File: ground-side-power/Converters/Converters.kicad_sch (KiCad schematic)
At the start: 29 parts, among them J10 Conn_01x03_Female, J11 Ground Connections, J12 Conn_01x04_Female, J13 DAQ Voltage Sensing, J14 DAQ Current Sensing, J27 Conn_01x02_Female, U1 TPS55340, U4 INA180, U5 INA180

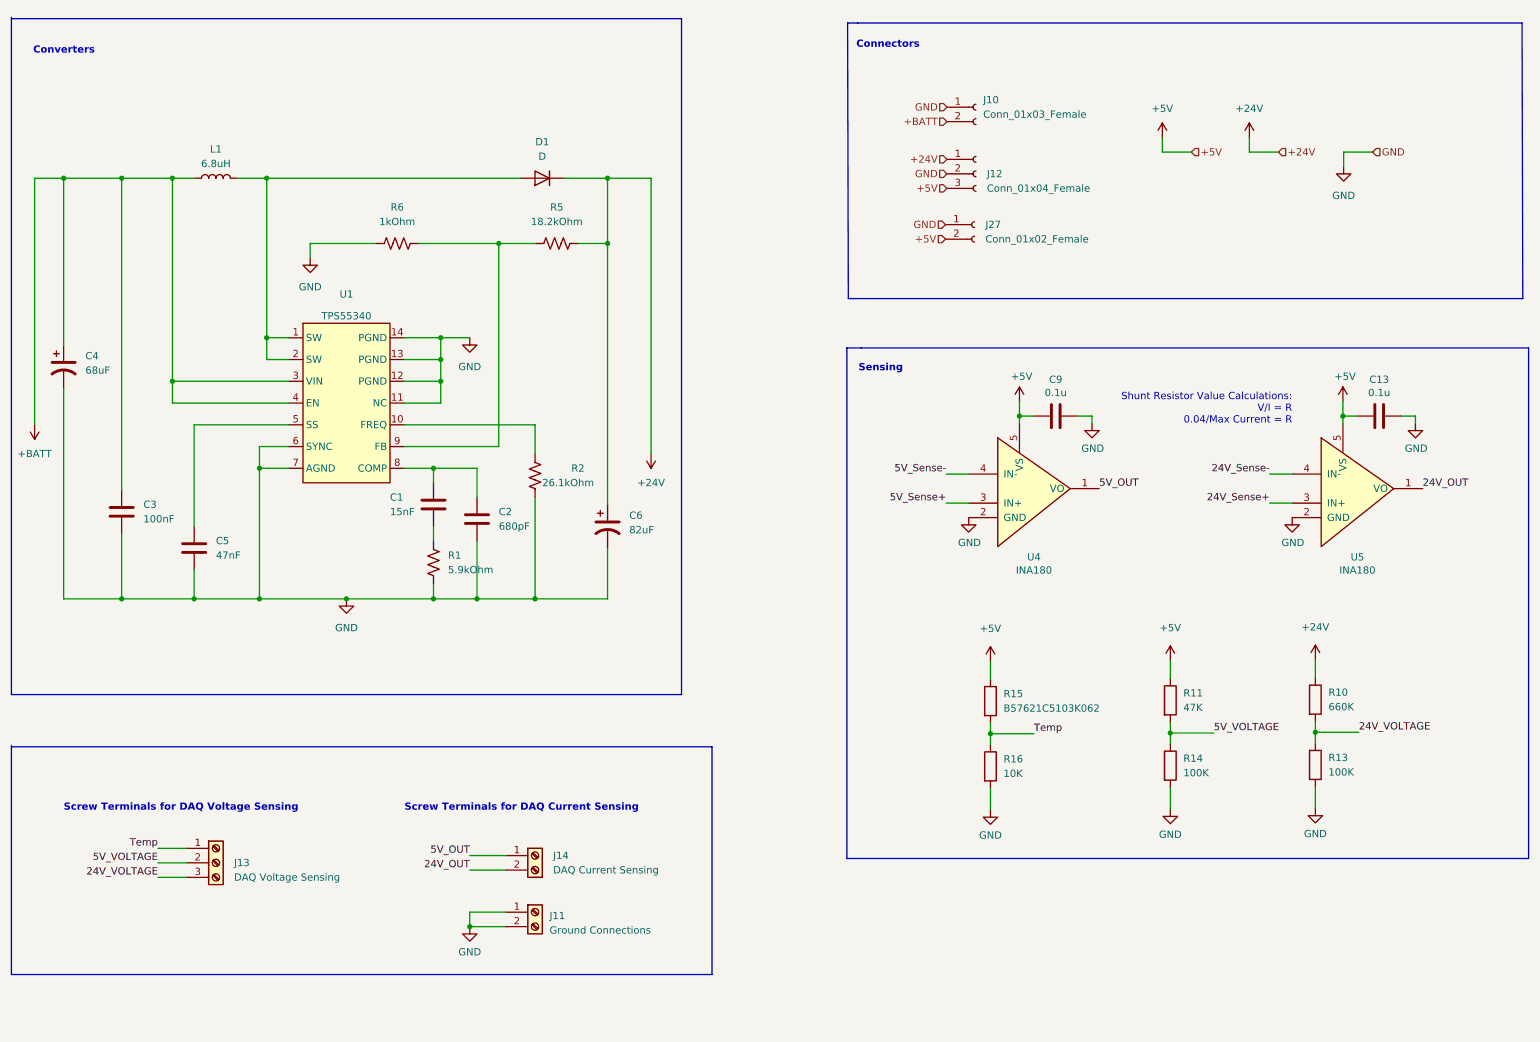
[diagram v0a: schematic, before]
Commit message: undeleted 5v regulator
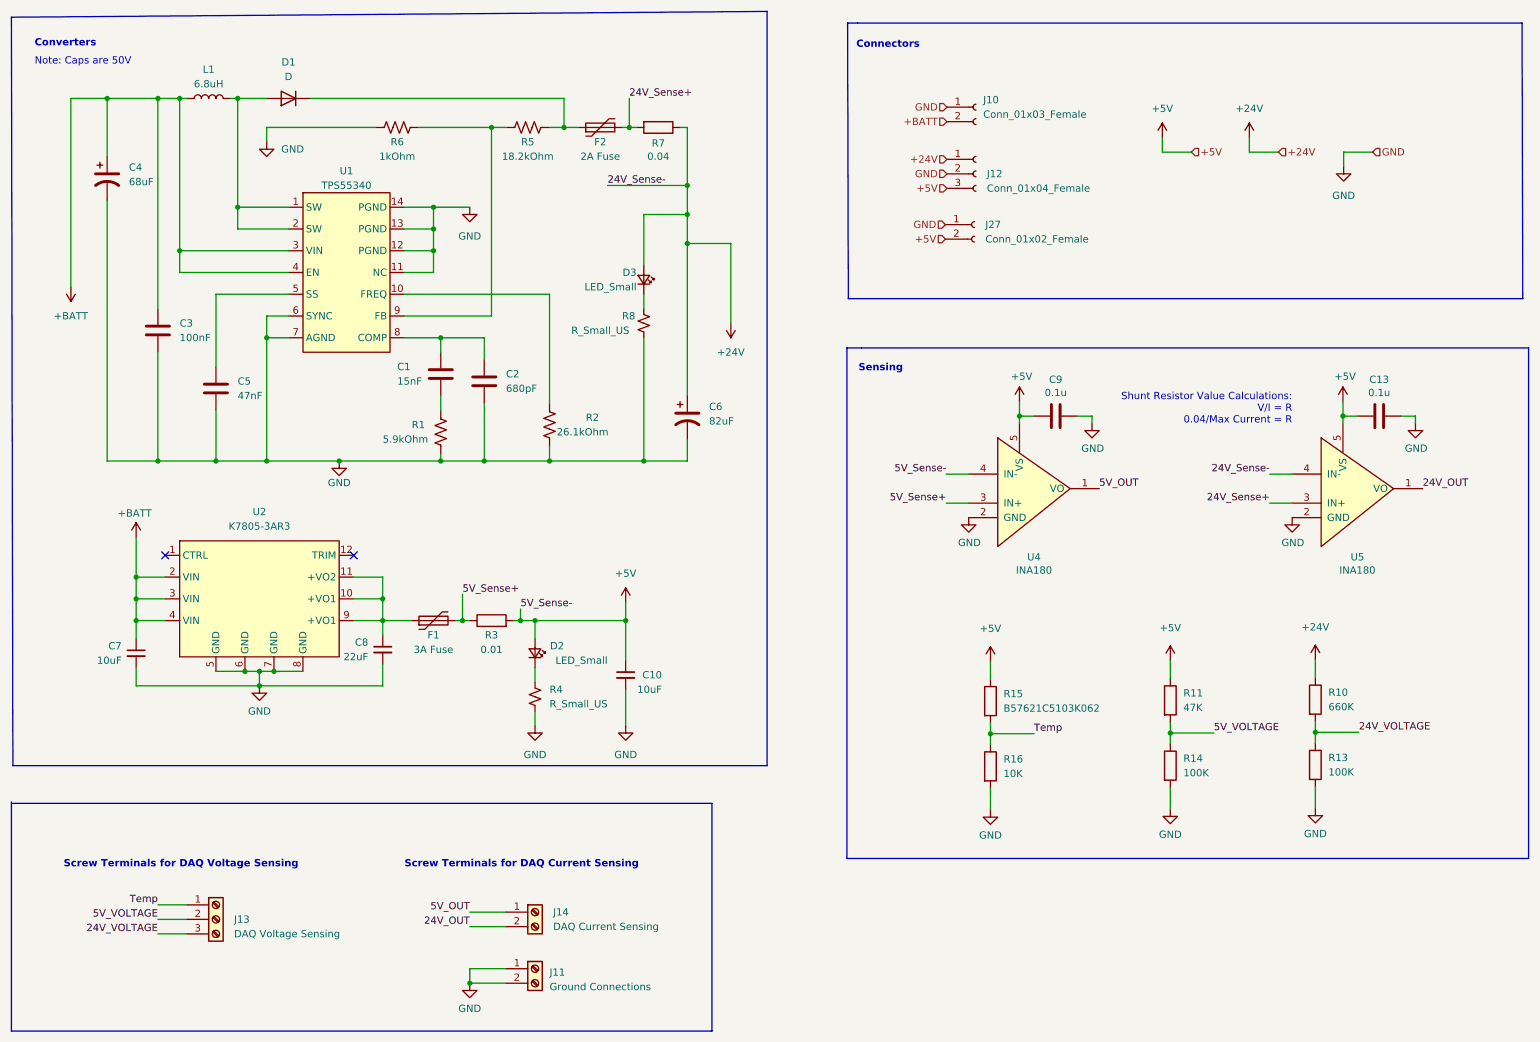
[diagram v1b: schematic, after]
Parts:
- added C10, C7: 10uF, Capacitor_SMD:C_0805_2012Metric_Pad1.18x1.45mm_HandSolder, symbol Device:C_Small
- added C8: 22uF, Capacitor_SMD:C_0805_2012Metric_Pad1.18x1.45mm_HandSolder, symbol Device:C_Small
- added D2, D3: LED_Small, Diode_SMD:D_1206_3216Metric_Pad1.42x1.75mm_HandSolder, symbol Device:LED_Small
- added F1: 3A Fuse, Fuse:Fuseholder_Clip-6.3x32mm_Littelfuse_102_122_Inline_P34.21x7.62mm_D1.98mm_Horizontal, symbol Device:Polyfuse
- added F2: 2A Fuse, Fuse:Fuseholder_Clip-6.3x32mm_Littelfuse_102_122_Inline_P34.21x7.62mm_D1.98mm_Horizontal, symbol Device:Polyfuse
- added R3: 0.01, Resistor_SMD:R_2512_6332Metric_Pad1.40x3.35mm_HandSolder, symbol Device:R
- added R4, R8: R_Small_US, Resistor_SMD:R_0805_2012Metric_Pad1.20x1.40mm_HandSolder, symbol Device:R_Small_US
- added R7: 0.04, Resistor_SMD:R_2512_6332Metric_Pad1.40x3.35mm_HandSolder, symbol Device:R
- added U2: K7805-3AR3, GSP:K7805-3AR3, symbol Regulator_Switching:AP63203WU
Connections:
- net 24V_Sense- is gone; now on net +24V: U5.4 (IN-)
- net 5V_Sense- is gone; now on net +5V: U4.4 (IN-)
- net +24V: now also D3.2 (A), R7.1; no longer D1.1 (K), R5.2
- net +5V: now also C10.1, D2.2 (A), R3.2
- net +BATT: now also C7.1, U2.2 (VIN), U2.3 (VIN), U2.4 (VIN)
- net 24V_Sense+: now also F2.2, R7.2
- net 5V_Sense+: now also F1.2, R3.1
- net GND: now also C10.2, C7.2, C8.2, R4.1, R8.1, U2.5 (GND), U2.6 (GND), U2.7 (GND), U2.8 (GND)
- new net: D2.1 (K), R4.2
- new net: C8.1, F1.1, U2.10 (+VO1), U2.11 (+VO2), U2.9 (+VO1)
- new net: D1.1 (K), F2.1, R5.2
- new net: D3.1 (K), R8.2
- no-connect marks 0 -> 2
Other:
- note added: "Note: Caps are 50V"
- moved on the sheet: C1, C2, C3, C4, C5, C6, D1, J11, J13, J14, L1, R1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

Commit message: implemented comments
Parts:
- removed C4: 68uF, Capacitor_SMD:C_Elec_6.3x7.7, symbol Device:C_Polarized_US
- removed C6: 82uF, Capacitor_SMD:CP_Elec_8x11.9, symbol Device:C_Polarized_US
- removed D1: D, Diode_SMD:D_SMB-SMC_Universal_Handsoldering, symbol Device:D
- removed D2, D3: LED_Small, Diode_SMD:D_1206_3216Metric_Pad1.42x1.75mm_HandSolder, symbol Device:LED_Small
- removed F1: 3A Fuse, Fuse:Fuseholder_Clip-6.3x32mm_Littelfuse_102_122_Inline_P34.21x7.62mm_D1.98mm_Horizontal, symbol Device:Polyfuse
- removed F2: 2A Fuse, Fuse:Fuseholder_Clip-6.3x32mm_Littelfuse_102_122_Inline_P34.21x7.62mm_D1.98mm_Horizontal, symbol Device:Polyfuse
- removed R10: 660K, Resistor_SMD:R_0805_2012Metric_Pad1.20x1.40mm_HandSolder, symbol Device:R
- removed R11: 47K, Resistor_SMD:R_0805_2012Metric_Pad1.20x1.40mm_HandSolder, symbol Device:R
- removed R13, R14: 100K, Resistor_SMD:R_0805_2012Metric_Pad1.20x1.40mm_HandSolder, symbol Device:R
- removed R15: B57621C5103K062, Resistor_SMD:R_1206_3216Metric_Pad1.30x1.75mm_HandSolder, symbol Device:R
- removed R16: 10K, Resistor_SMD:R_0805_2012Metric_Pad1.20x1.40mm_HandSolder, symbol Device:R
- removed R3: 0.01, Resistor_SMD:R_2512_6332Metric_Pad1.40x3.35mm_HandSolder, symbol Device:R
- removed R4, R8: R_Small_US, Resistor_SMD:R_0805_2012Metric_Pad1.20x1.40mm_HandSolder, symbol Device:R_Small_US
- removed R7: 0.04, Resistor_SMD:R_2512_6332Metric_Pad1.40x3.35mm_HandSolder, symbol Device:R
- added C11, C4, C6: 4.7uF, Capacitor_SMD:C_0805_2012Metric_Pad1.18x1.45mm_HandSolder, symbol Device:C
- added D2: SK54A-LTP, symbol Device:D_Schottky
- added D4, D5: LED, symbol Device:LED
- added F3: 0685T4000-01, symbol Device:Fuse
- added F4: 3A Fuse, symbol Device:Fuse
- added R10: 0.01R, symbol Device:R_US
- added R12: 78.7k, symbol Device:R_US
- added R17: 10k, symbol Device:R_US
- added R18: 187k, symbol Device:R_US
- added R19: 660k, symbol Device:R_US
- added R20: 100k, symbol Device:R_US
- added R3: 16mR, symbol Device:R_US
- added R4: 2k, symbol Device:R_US
- added R8, R9: R_US, symbol Device:R_US
- C1: value 15nF -> 0.1uF
- C2: value 680pF -> 100pF
- C3: value 100nF -> 10uF
- L1: value 6.8uH -> 74437368100
- R1: value 5.9kOhm -> B57621C5103K062; footprint Resistor_SMD:R_0402_1005Metric_Pad0.72x0.64mm_HandSolder -> (none)
- R2: value 26.1kOhm -> 10k; footprint Resistor_SMD:R_0402_1005Metric_Pad0.72x0.64mm_HandSolder -> (none)
- R5: value 18.2kOhm -> 47k; footprint Resistor_SMD:R_0402_1005Metric_Pad0.72x0.64mm_HandSolder -> (none)
- R6: value 1kOhm -> 100k; footprint Resistor_SMD:R_0402_1005Metric_Pad0.72x0.64mm_HandSolder -> (none)
- U1: footprint Package_SO:TSSOP-14_4.4x3.6mm_P0.4mm -> (none)
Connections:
- net +24V: now also D4.2 (A), R19.1, R3.2
- net +5V: now also R1.1, R5.1, D5.2 (A), R10.2
- net 24V_Sense+: now also F3.2, R3.1
- net 24V_VOLTAGE: now also R19.2, R20.1
- net 5V_Sense+: now also F4.2, R10.1
- net 5V_VOLTAGE: now also R5.2, R6.1
- net GND: now also R6.2, C11.2, C4.2, C6.2, R12.2, R17.2, R20.2, R4.2, R8.2, R9.2; no longer R1.2, R6.1
- net Temp: now also R1.2, R2.1
- net at C1.2: now also R4.1; no longer R1.1
- net at C8.1, U2.10 (+VO1), U2.11 (+VO2)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: now also F4.1
- net at L1.2, U1.1 (SW), U1.2 (SW): now also D2.2 (A)
- net at U1.10 (FREQ): now also R12.1; no longer R2.1
- new net: R17.1, R18.1, U1.9 (FB)
- new net: C11.1, C4.1, C6.1, D2.1 (K), F3.1, R18.2
- new net: D4.1 (K), R9.1
- new net: D5.1 (K), R8.1
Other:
- moved on the sheet: C1, C10, C2, C3, C5, C7, C8, L1, U2

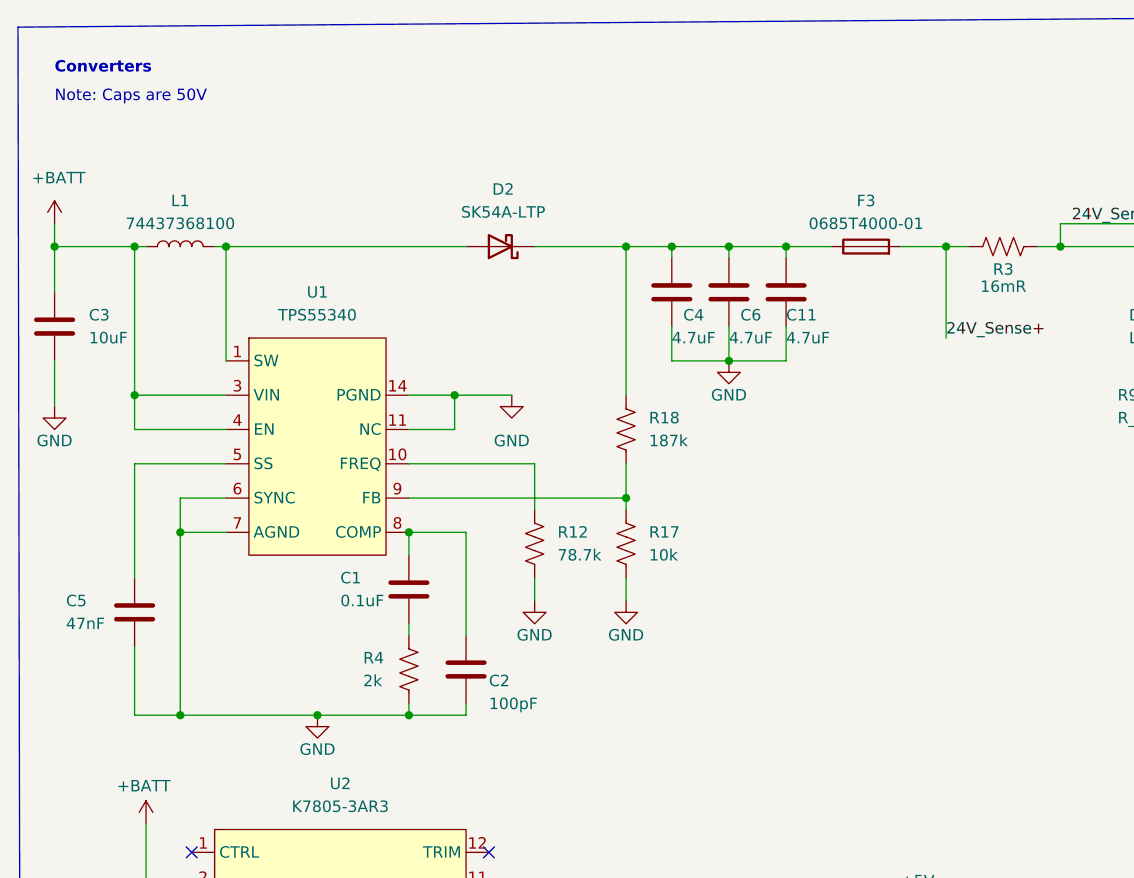
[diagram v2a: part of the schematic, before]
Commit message: updatad symbols with correct values
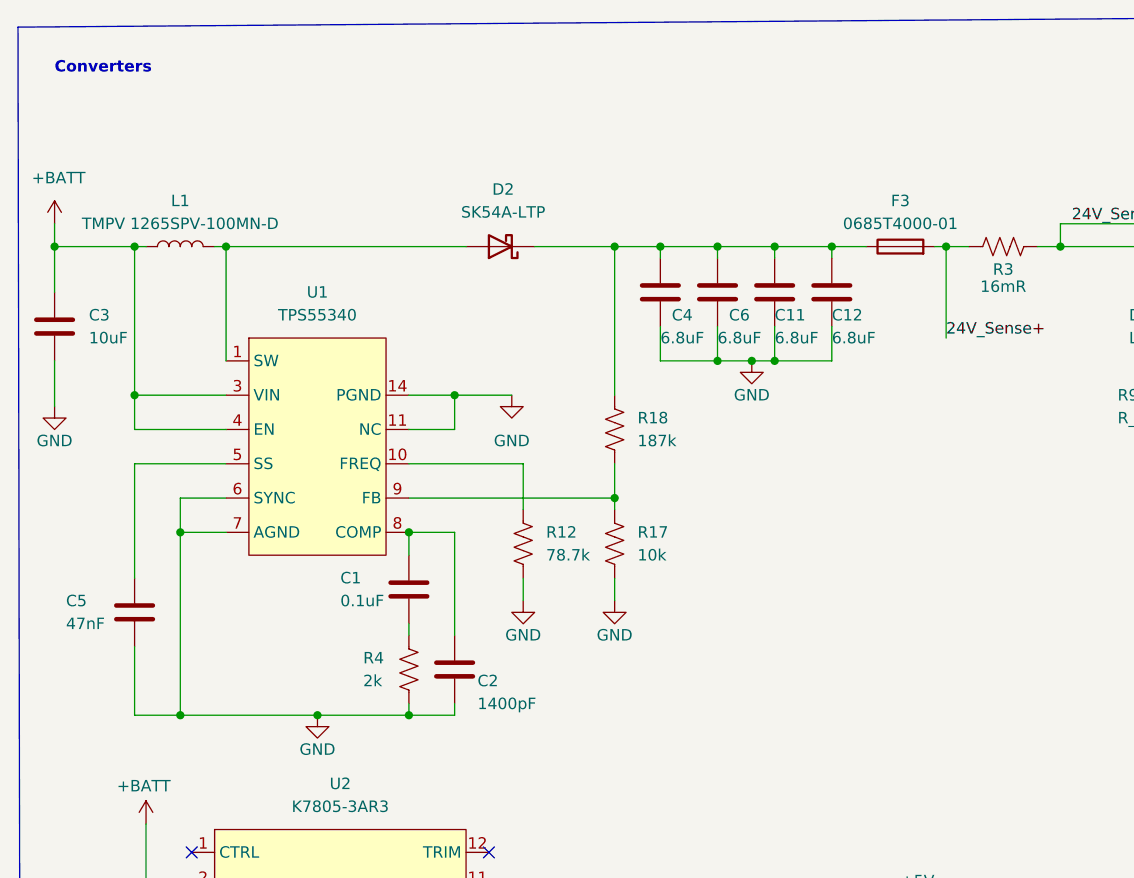
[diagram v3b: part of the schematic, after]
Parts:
- added C12: 6.8uF, Capacitor_SMD:C_0805_2012Metric_Pad1.18x1.45mm_HandSolder, symbol Device:C
- C11, C4, C6: value 4.7uF -> 6.8uF
- C2: value 100pF -> 1400pF
- L1: value 74437368100 -> TMPV 1265SPV-100MN-D
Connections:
- net GND: now also C12.2
- net at C11.1, C4.1, C6.1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: now also C12.1
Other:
- note removed: "Note: Caps are 50V"
- moved on the sheet: C11, C2, C4, C6, F3, R12, R17, R18
